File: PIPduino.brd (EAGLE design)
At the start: 46 x 46 mm, 45 parts, among them IC1 ATmega328P\, J1 ISP|SPI, U1 NCP5500, X1 16MHz

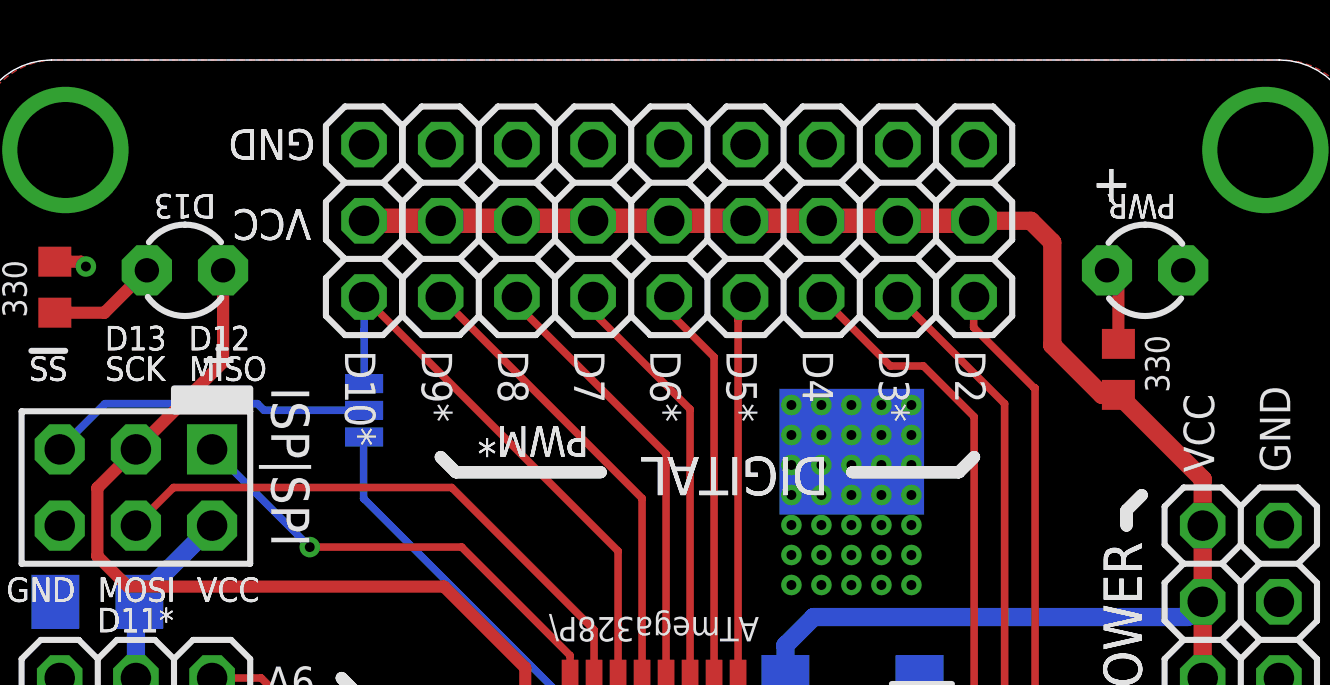
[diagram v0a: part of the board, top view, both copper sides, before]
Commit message: Fixed some silk errors
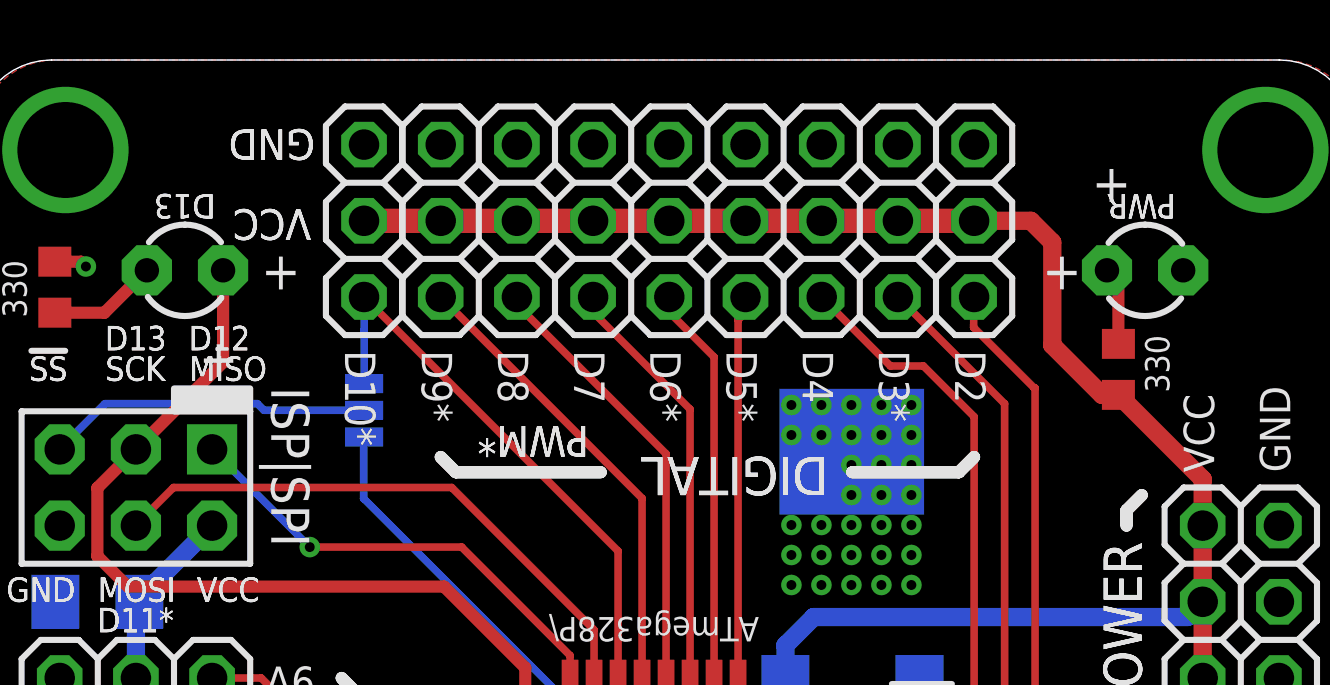
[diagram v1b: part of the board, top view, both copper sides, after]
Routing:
- net GND: vias 48 -> 44
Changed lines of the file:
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@@
 <text x="37.155" y="16.09" size="2.54" layer="26" font="vector" ratio="12" rot="MR0">PIPduino</text>
 <text x="37.074" y="14.131" size="1.27" layer="26" font="vector" ratio="12" rot="MR0">Put In Project</text>
-<text x="10.162" y="42.404" size="1.016" layer="28" font="vector" ratio="12" rot="MR0">#4/M3</text>
-<text x="0.362" y="13.79" size="1.016" layer="28" font="vector" ratio="12" rot="MR90">Holes on 40cm square</text>
+<text x="10.416" y="43.42" size="1.016" layer="28" font="vector" ratio="12" rot="MR0">#4/M3</text>
+<text x="23.929" y="44.685" size="1.016" layer="28" font="vector" ratio="12" rot="MR0">Holes on 40cm square</text>
 <text x="11.706" y="33.786" size="1.016" layer="26" font="vector" ratio="12" rot="MR0">!SS</text>
 <text x="3.505" y="34.3" size="1.016" layer="26" font="vector" ratio="12" rot="MR0">!SS</text>
@@
 <wire x1="6.985" y1="40.513" x2="5.782009375" y2="39.92460625" width="0.2032" layer="121" curve="52.126411"/>
 <wire x1="8.18799375" y1="39.924609375" x2="6.985" y2="40.513003125" width="0.2032" layer="121" curve="52.126391"/>
-<text x="8.763" y="36.703" size="1.27" layer="121" font="vector" ratio="16" rot="R180">+</text>
+<text x="9.525" y="38.354" size="1.27" layer="121" font="vector" ratio="16">+</text>
 <wire x1="19.11700625" y1="17.577003125" x2="19.11700625" y2="24.586996875" width="0.2032" layer="121"/>
 <wire x1="19.11700625" y1="24.586996875" x2="26.127" y2="24.586996875" width="0.2032" layer="121"/>
@@
 <wire x1="38.989" y1="37.465" x2="40.191990625" y2="38.05339375" width="0.2032" layer="121" curve="52.126411"/>
 <wire x1="37.78600625" y1="38.053390625" x2="38.989" y2="37.464996875" width="0.2032" layer="121" curve="52.126391"/>
-<text x="37.211" y="41.275" size="1.27" layer="121" font="vector" ratio="16">+</text>
+<text x="35.56" y="38.354" size="1.27" layer="121" font="vector" ratio="16">+</text>
 <wire x1="14.299996875" y1="13.3" x2="18.2999875" y2="13.3" width="0.2032" layer="121"/>
 <wire x1="18.2999875" y1="10.30000625" x2="14.299996875" y2="10.30000625" width="0.2032" layer="121"/>
@@
 <text x="38.989" y="36.83" size="0.8128" layer="121" font="vector" ratio="25" rot="R270">330</text>
 <text x="14.36799375" y="13.697990625" size="1.016" layer="121" font="vector" ratio="20">RESET</text>
-<text x="10.16200625" y="42.404003125" size="1.016" layer="122" font="vector" ratio="20" rot="MR0">#4/M3</text>
-<text x="0.362" y="13.789990625" size="1.016" layer="122" font="vector" ratio="20" rot="MR90">Holes on 40cm square</text>
+<text x="10.41600625" y="43.420003125" size="1.016" layer="122" font="vector" ratio="20" rot="MR0">#4/M3</text>
+<text x="23.929009375" y="44.685" size="1.016" layer="122" font="vector" ratio="20" rot="MR0">Holes on 40cm square</text>
 <text x="28.059990625" y="20.592009375" size="0.8128" layer="122" font="vector" ratio="25" rot="MR90">106</text>
 <text x="35.56" y="20.647990625" size="0.8128" layer="122" font="vector" ratio="25" rot="MR90">106</text>
@@
 <via x="30.2" y="31.5" extent="1-16" drill="0.3302"/>
 <via x="29.2" y="31.5" extent="1-16" drill="0.3302"/>
-<via x="28.2" y="31.5" extent="1-16" drill="0.3302"/>
-<via x="28.2" y="32.5" extent="1-16" drill="0.3302"/>
-<via x="27.2" y="32.5" extent="1-16" drill="0.3302"/>
-<via x="27.2" y="31.5" extent="1-16" drill="0.3302"/>
 <via x="27.2" y="30.5" extent="1-16" drill="0.3302"/>
 <via x="28.2" y="30.5" extent="1-16" drill="0.3302"/>

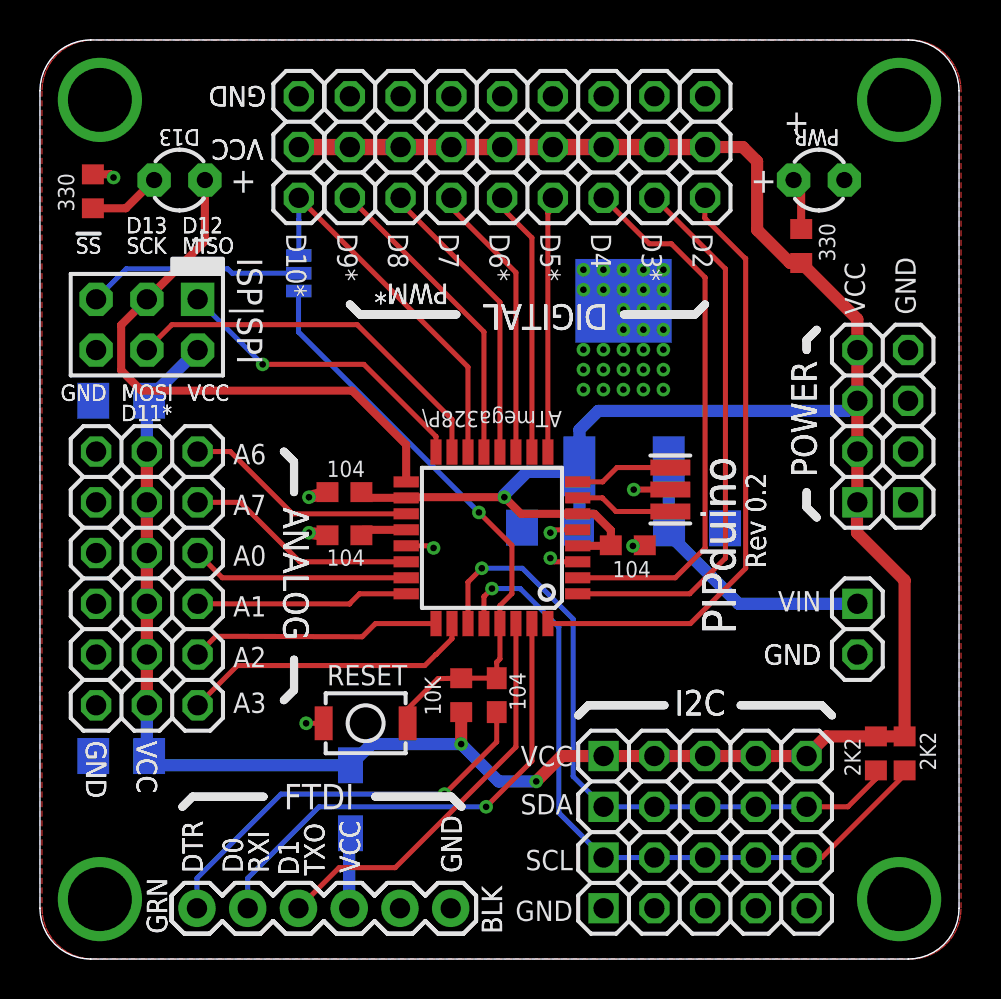
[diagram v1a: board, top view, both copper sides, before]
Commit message: Improved thermal design, minor silk fixes, revised LED design for 330 ohm reflow DFM
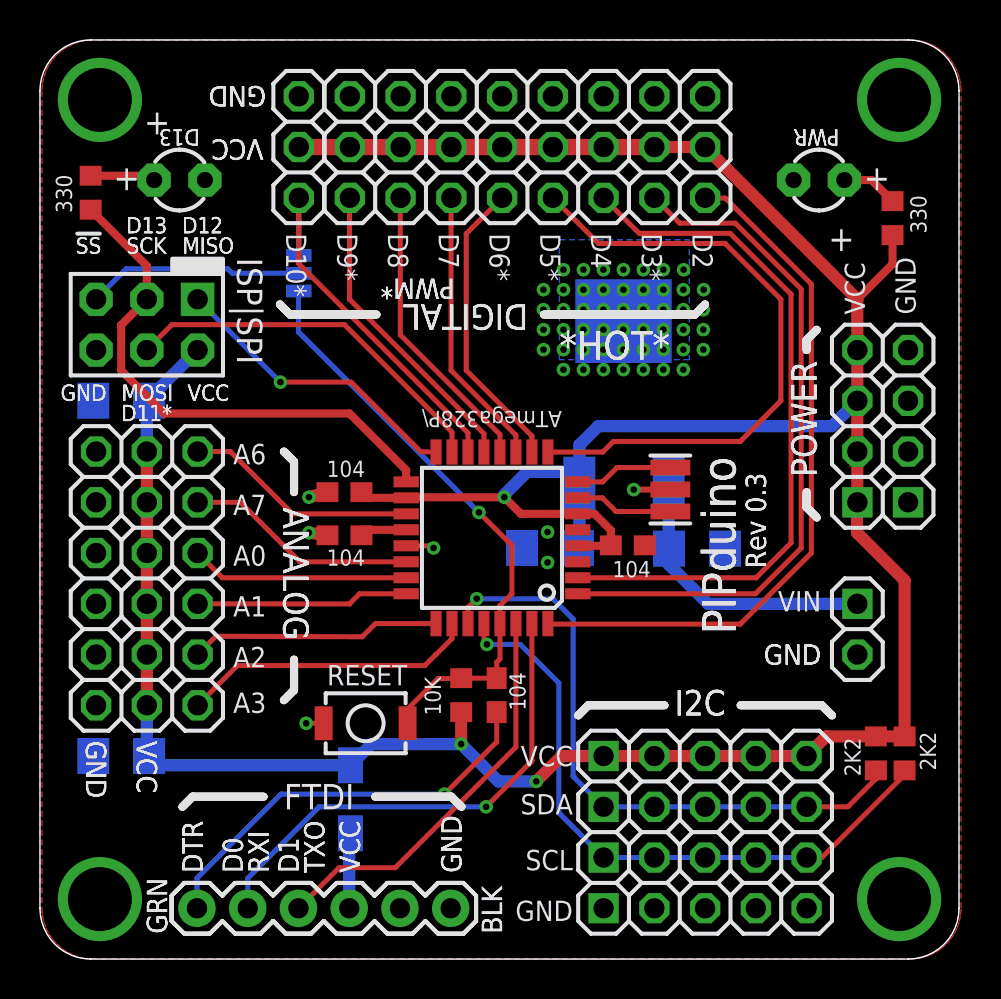
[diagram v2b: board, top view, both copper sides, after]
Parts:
- moved R5 4.78 mm to (42.7, 37.1)
- moved U1 1.02 mm to (29.2, 27.3)
- moved C2 1.02 mm to (25.5, 20.6)
- moved C5 1.02 mm to (32.9, 20.5)
- moved R3 0.13 mm to (2.54, 38.4)
- turned D13 to 0 degrees
- turned PWR to 180 degrees
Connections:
- net GND: now also D13.K; no longer R3.1
- net N$1: now also D13.A, R3.1; no longer D13.K, R3.2
- net SCK: now also R3.2; no longer D13.A
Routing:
- net D5: track 12.8 -> 31.3 mm
- net D4: track 27.3 -> 35.2 mm
- net D3: track 27.6 -> 34.3 mm
- net D2: track 30.5 -> 35.2 mm
- net GND: track 11.3 -> 6.82 mm, vias 44 -> 61
- net VCC: track 158.9 -> 162.5 mm
- net SCL: track 35.5 -> 32.2 mm
- net SCK: track 28.9 -> 26.7 mm
- net SDA: track 33.3 -> 31.3 mm
- net D6: track 13.3 -> 14.8 mm
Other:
- board text added: "*HOT*"
- board text added: "Rev 0.3"
- board text removed: "Rev 0.2"
